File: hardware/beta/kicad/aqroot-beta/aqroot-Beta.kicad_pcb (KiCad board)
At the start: 4 copper layers, 74 x 155 mm, 187 parts, among them J1 CH280QV10-CT_50P, J2 Molex_5025700893, J3 USB_C_Receptacle_USB2.0_16P, J4 JST-PH-2 BATTERY, J5 COMMUNITY_HEADER_2x13, J6 JST-PH-2 SPEAKER, Q1 AO3400A, SW1 BOOT, SW2 UP, SW3 DOWN, SW4 LEFT, SW5 RIGHT, SW6 A_SELECT, SW7 B_BACK, SW8 HOME, SW9 SW_SPDT, U1 ESP32-S3-WROOM-1, U10 USBLC6-2SC6, U11 BQ25185, U12 TPS63020, U13 TPS61023, U14 MAX17048, U15 TPS22918, U16 TCA9517ADGK, U17 TPS61169DCKR, U2 TCA9535PWR, U3 TCA9535PWR, U4 BMI270, U5 MAX98357A, U6 TSOP38238, U7 E07-400M10S, U8 E22-900M22S, U9 ST25R3916-AQET

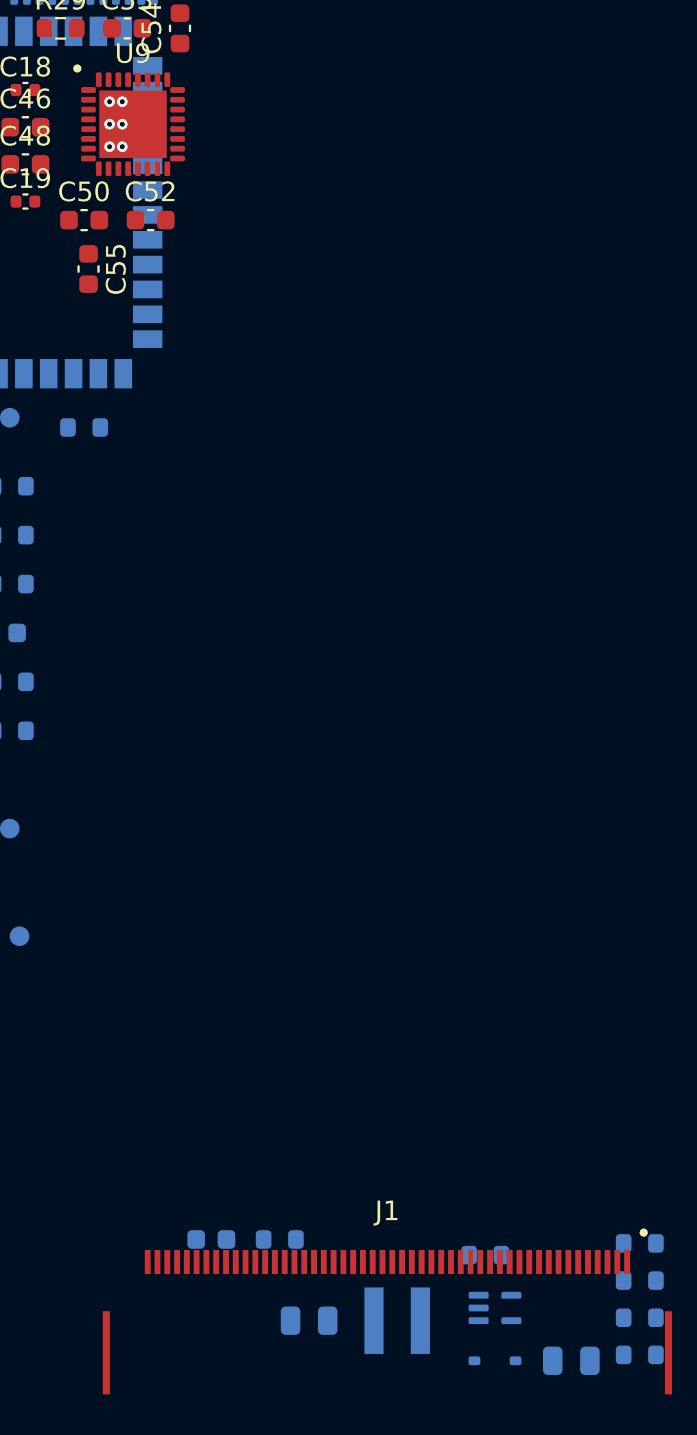
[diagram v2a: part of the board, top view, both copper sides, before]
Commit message: AQROOT Beta: close routing blockers, add U17 VIN bypass
Closes the three blockers from the Routing Pass 1 partial. No routing was
performed; GND remains the only net carrying copper.

BAT/SYS width lock, per CTO ruling. IBAT_OCP 3.125 A is a fault trip
threshold, not a routing design current, and the floor derived from it
made U11's 0.40 mm pitch west flank unroutable. BAT_MAIN min 1.00/opt
1.50 -> min 0.60/opt 1.00 mm (1.5 A sustained, 1 oz outer, dT=10 K needs
0.525 mm). SYS_MAIN min 0.60/opt 1.00 -> min 0.50/opt 0.80 mm. Netclass
defaults follow. The wrong derivation is corrected in the rule comment so
it stops propagating. Layer policy is now written into the file: both
rails are outer-layer by policy, BAT_MAIN must not distribute on In2
(1.5 A at 0.5 oz needs 2.73 mm), and an outer width must never be
inherited onto inner copper. Necking rule unchanged, still in the
PRECEDENCE TAIL. Zero RF/E4/E5 rule lines touched.

HEADER RESERVED In1 void removed. The audit found only J5 inside it - 26
THT pads, five of them GND - and no manufacturer requirement for an In1
void. Layer set F.Cu+In1+In2+B.Cu -> F.Cu+In2+B.Cu. In1 fill 10025.8 ->
10237.0 mm2, +211.3 mm2 (+2.11%), now 91.56% of outline. The 37 x 8.5 mm
slot in the reference plane is gone and J5's five GND pins now tie
directly to the pour. ST AN5240 Rev 5 section 4.2 corroborates: "avoiding
slots in the ground plane". J5 not moved. No new DRC issue.

U9 exposed-pad grounding audited against ST AN5240 Rev 5 section 8,
retrieved via browser because curl and WebFetch both fail against st.com,
and because the archived DS12484 datasheet has no layout guidance at all.
ST asks for the pad to be tied to the ground plane by "multiple
through-vias" to "keep the total parasitic inductance low", gives no
count and no pattern, and imposes no symmetry requirement on the thermal
pad - all seven symmetry mentions in AN5240 concern the RFO/RFI
differential traces and matching network. ST's Figure 16 shows 3x3 = 9
vias as a refer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
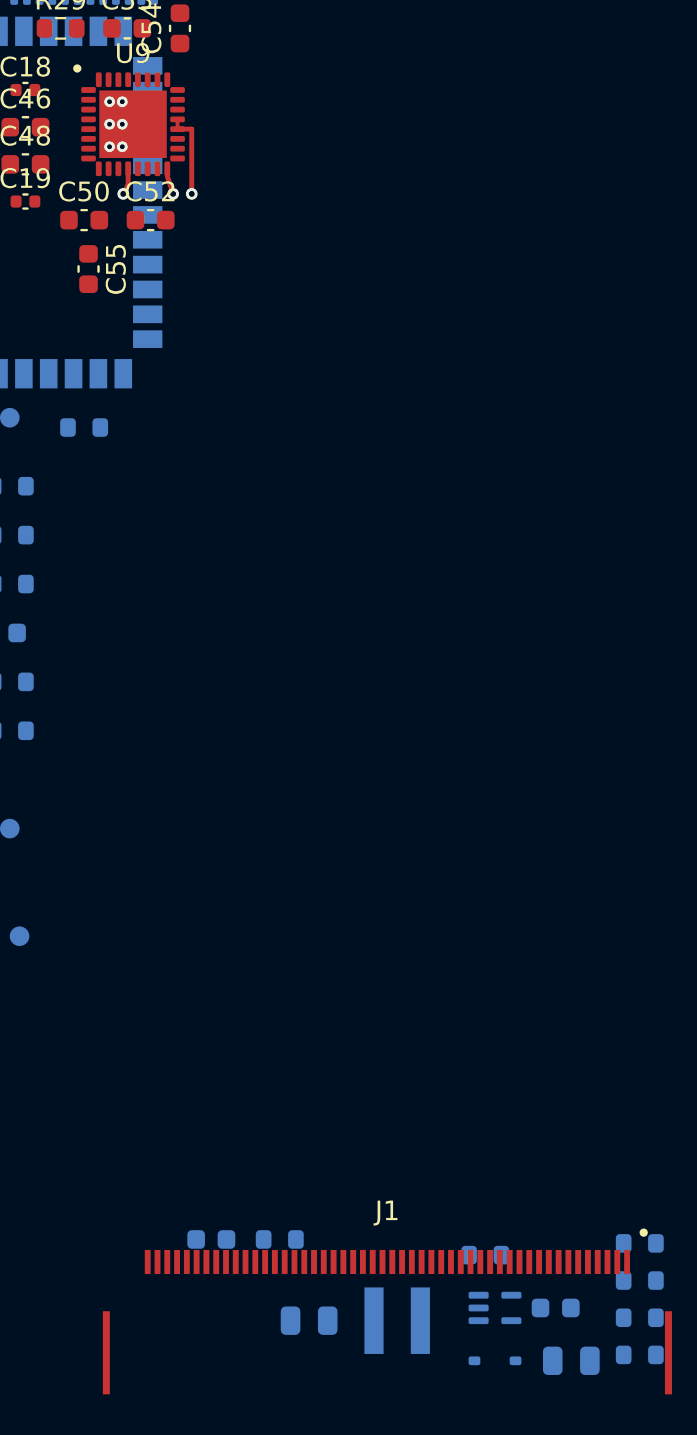
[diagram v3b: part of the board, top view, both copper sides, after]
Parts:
- added C56: 100nF, C_0603_1608Metric, B.Cu at (46.1, 82.5)
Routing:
- net GND: track 3.20 -> 9.67 mm, vias 18 -> 21
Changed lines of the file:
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@@
 	(footprint "C_0603_1608Metric"
 		(layer "F.Cu")
-		(at 22.225 29.4 -90)
+		(at 22 26.9)
 		(descr "Capacitor SMD 0603 (1608 Metric), square (rectangular) end terminal, IPC-7351 nominal, (Body size source: IPC-SM-782 page 76, https://www.pcb-3d.com/wordpress/wp-content/uploads/ipc-sm-782a_amendment_1_and_2.pdf)")
 		(tags "capacitor")
-		(property "Reference" "C55"
-			(at 0 -1.43 270)
+		(property "Reference" "C50"
+			(at 0 -1.43 0)
 			(layer "F.SilkS")
 			(effects
@@
 			)
 		)
-		(property "Value" "2.2uF"
-			(at 0 1.43 270)
+		(property "Value" "10nF"
+			(at 0 1.43 0)
 			(layer "F.Fab")
 			(effects
@@
 		)
 		(property "Datasheet" ""
-			(at 0 0 270)
+			(at 0 0 0)
 			(layer "F.Fab")
 			(hide yes)
@@
 		)
 		(property "Description" ""
-			(at 0 0 270)
+			(at 0 0 0)
 			(layer "F.Fab")
 			(hide yes)
@@
 		)
 		(property "KiLib_Generator" "SMD_2terminal_chip_molded"
-			(at 0 0 270)
+			(at 0 0 0)
 			(layer "F.SilkS")
 			(hide yes)
@@
 		(duplicate_pad_numbers_are_jumpers no)
 		(fp_line
-			(start -0.14058 0.51)
-			(end 0.14058 0.51)
+			(start -0.14058 -0.51)
+			(end 0.14058 -0.51)
 			(stroke
 				(width 0.12)
@@
 		)
 		(fp_line
-			(start -0.14058 -0.51)
-			(end 0.14058 -0.51)
+			(start -0.14058 0.51)
+			(end 0.14058 0.51)
 			(stroke
 				(width 0.12)
@@
 		)
 		(fp_text user "${REFERENCE}"
-			(at 0 0 270)
+			(at 0 0 0)
 			(layer "F.Fab")
 			(effects
@@
 		)
 		(pad "1" smd roundrect
-			(at -0.775 0 270)
+			(at -0.775 0)
 			(size 0.9 0.95)
 			(layers "F.Cu" "F.Mask" "F.Paste")
 			(roundrect_rratio 0.25)
-			(net "/NFC_5V_PA_PENDING")
+			(net "/04_SPI_B_RADIOS_NFC/NFC_VDD_RF")
 		)
 		(pad "2" smd roundrect
-			(at 0.775 0 270)
+			(at 0.775 0)
 			(size 0.9 0.95)
 			(layers "F.Cu" "F.Mask" "F.Paste")
@@
 	(footprint "C_0603_1608Metric"
 		(layer "F.Cu")
-		(at 22 26.9)
+		(at 22.225 29.4 -90)
 		(descr "Capacitor SMD 0603 (1608 Metric), square (rectangular) end terminal, IPC-7351 nominal, (Body size source: IPC-SM-782 page 76, https://www.pcb-3d.com/wordpress/wp-content/uploads/ipc-sm-782a_amendment_1_and_2.pdf)")
 		(tags "capacitor")
-		(property "Reference" "C50"
-			(at 0 -1.43 0)
+		(property "Reference" "C55"
+			(at 0 -1.43 270)
 			(layer "F.SilkS")
 			(effects
@@
 			)
 		)
-		(property "Value" "10nF"
-			(at 0 1.43 0)
+		(property "Value" "2.2uF"
+			(at 0 1.43 270)
 			(layer "F.Fab")
 			(effects
@@
 		)
 		(property "Datasheet" ""
-			(at 0 0 0)
+			(at 0 0 270)
 			(layer "F.Fab")
 			(hide yes)
@@
 		)
 		(property "Description" ""
-			(at 0 0 0)
+			(at 0 0 270)
 			(layer "F.Fab")
 			(hide yes)
@@
 		)
 		(property "KiLib_Generator" "SMD_2terminal_chip_molded"
-			(at 0 0 0)
+			(at 0 0 270)
 			(layer "F.SilkS")
 			(hide yes)
@@
 		(duplicate_pad_numbers_are_jumpers no)
 		(fp_line
-			(start -0.14058 -0.51)
-			(end 0.14058 -0.51)
+			(start -0.14058 0.51)
+			(end 0.14058 0.51)
 			(stroke
 				(width 0.12)
@@
 		)
 		(fp_line
-			(start -0.14058 0.51)
-			(end 0.14058 0.51)
+			(start -0.14058 -0.51)
+			(end 0.14058 -0.51)
 			(stroke
 				(width 0.12)
@@
 		)
 		(fp_text user "${REFERENCE}"
-			(at 0 0 0)
+			(at 0 0 270)
 			(layer "F.Fab")
 			(effects
@@
 		)
 		(pad "1" smd roundrect
-			(at -0.775 0)
+			(at -0.775 0 270)
 			(size 0.9 0.95)
 			(layers "F.Cu" "F.Mask" "F.Paste")
 			(roundrect_rratio 0.25)
-			(net "/04_SPI_B_RADIOS_NFC/NFC_VDD_RF")
+			(net "/NFC_5V_PA_PENDING")
 		)
 		(pad "2" smd roundrect
-			(at 0.775 0)
+			(at 0.775 0 270)
 			(size 0.9 0.95)
 			(layers "F.Cu" "F.Mask" "F.Paste")
@@
 		)
 	)
+	(footprint "C_0603_1608Metric"
+		(layer "B.Cu")
+		(at 46.1 82.5)
+		(descr "Capacitor SMD 0603 (1608 Metric), square (rectangular) end terminal, IPC-7351 nominal, (Body size source: IPC-SM-782 page 76, https://www.pcb-3d.com/wordpress/wp-content/uploads/ipc-sm-782a_amendment_1_and_2.pdf)")
+		(tags "capacitor")
+		(property "Reference" "C56"
+			(at 0 1.43 180)
+			(layer "B.SilkS")
+			(effects
+				(font
+					(size 1 1)
+					(thickness 0.15)
+				)
+				(justify mirror)
+			)
+		)
+		(property "Value" "100nF"
+			(at 0 -1.43 180)
+			(layer "B.Fab")
+			(effects
+				(font
+					(size 1 1)
+					(thickness 0.15)
+				)
+				(justify mirror)
+			)
+		)
+		(property "Datasheet" ""
+			(at 0 0 180)
+			(layer "B.Fab")
+			(hide yes)
+			(effects
+				(font
+					(size 1.27 1.27)
+				)
+				(justify mirror)
+			)
+		)
+		(property "Description" ""
+			(at 0 0 180)
+			(layer "B.Fab")
+			(hide yes)
+			(effects
+				(font
+					(size 1.27 1.27)
+				)
+				(justify mirror)
+			)
+		)
+		(property "KiLib_Generator" "SMD_2terminal_chip_molded"
+			(at 0 0 180)
+			(layer "B.SilkS")
+			(hide yes)
+			(effects
+				(font
+					(size 1 1)
+					(thickness 0.15)
+				)
+				(justify mirror)
+			)
+		)
+		(attr smd)
+		(duplicate_pad_numbers_are_jumpers no)
+		(fp_line
+			(start -0.14058 -0.51)
+			(end 0.14058 -0.51)
+			(stroke
+				(width 0.12)
+				(type solid)
+			)
+			(layer "B.SilkS")
+		)
+		(fp_line
+			(start -0.14058 0.51)
+			(end 0.14058 0.51)
+			(stroke
+				(width 0.12)
+				(type solid)
+			)
+			(layer "B.SilkS")
+		)
+		(fp_rect
+			(start -1.48 0.73)
+			(end 1.48 -0.73)
+			(stroke
+				(width 0.05)
+				(type solid)
+			)
+			(fill no)
+			(layer "B.CrtYd")
+		)
+		(fp_rect
+			(start -0.8 0.4)
+			(end 0.8 -0.4)
+			(stroke
+				(width 0.1)
+				(type solid)
+			)
+			(fill no)
+			(layer "B.Fab")
+		)
+		(fp_text user "${REFERENCE}"
+			(at 0 0 180)
+			(layer "B.Fab")
+			(effects
+				(font
+					(size 0.4 0.4)
+					(thickness 0.06)
+				)
+				(justify mirror)
+			)
+		)
+		(pad "1" smd roundrect
+			(at -0.775 0)
+			(size 0.9 0.95)
+			(layers "B.Cu" "B.Mask" "B.Paste")
+			(roundrect_rratio 0.25)
+			(net "+3V3")
+		)
+		(pad "2" smd roundrect
+			(at 0.775 0)
+			(size 0.9 0.95)
+			(layers "B.Cu" "B.Mask" "B.Paste")
+			(roundrect_rratio 0.25)
+			(net "GND")
+		)
+		(embedded_fonts no)
+		(model "${KICAD10_3DMODEL_DIR}/Capacitor_SMD.3dshapes/C_0603_1608Metric.step"
+			(offset
+				(xyz 0 0 0)
+			)
+			(scale
+				(xyz 1 1 1)
+			)
+			(rotate
+				(xyz 0 0 0)
+			)
+		)
+	)
 	(footprint "Resistor_SMD:R_0603_1608Metric"
 		(layer "B.Cu")
@@
 	)
 	(segment
+		(start 24.25 24.65)
+		(end 24.25 25.1)
+		(width 0.25)
+		(layer "F.Cu")
+		(net "GND")
+	)
+	(segment
 		(start 63.9 67.4)
 		(end 63.9 67.8)
@@
 	)
 	(segment
+		(start 26.775 22.25)
+		(end 27.5 22.25)
+		(width 0.25)
+		(layer "F.Cu")
+		(net "GND")
+	)
+	(segment
 		(start 64.5 52.4)
 		(end 64.5 53.9)
@@
 	)
 	(segment
+		(start 26.775 21.75)
+		(end 26.775 22.25)
+		(width 0.2)
+		(layer "F.Cu")
+		(net "GND")
+	)
+	(segment
 		(start 63.9 67.8)
 		(end 62.6 67.8)
@@
 		(net "GND")
 	)
+	(segment
+		(start 24.25 25.1)
+		(end 24 25.56)
+		(width 0.25)
+		(layer "F.Cu")
+		(net "GND")
+	)
+	(segment
+		(start 26.25 24.65)
+		(end 26.55 25.56)
+		(width 0.25)
+		(layer "F.Cu")
+		(net "GND")
+	)
+	(segment
+		(start 27.5 22.25)
+		(end 27.5 25.56)
+		(width 0.25)
+		(layer "F.Cu")
+		(net "GND")
+	)
 	(via
 		(at 62.5 14.8)
@@
 	)
 	(via
+		(at 27.5 25.56)
+		(size 0.6)
+		(drill 0.3)
+		(layers "F.Cu" "B.Cu")
+		(net "GND")
+	)
+	(via
 		(at 64.5 80.5)
 		(size 0.55)
@@
 	)
 	(via
+		(at 24 25.56)
+		(size 0.6)
+		(drill 0.3)
+		(layers "F.Cu" "B.Cu")
+		(net "GND")
+	)
+	(via
 		(at 65.5 50.65)
 		(size 0.55)
@@
 		(net "GND")
 	)
+	(via
+		(at 26.55 25.56)
+		(size 0.6)
+		(drill 0.3)
+		(layers "F.Cu" "B.Cu")
+		(net "GND")
+	)
 	(zone
 		(layers "F.Cu" "B.Cu" "In1.Cu" "In2.Cu")
-		(name "HEADER RESERVED")
+		(name "NFC RESERVED")
 		(hatch edge 0.5)
 		(connect_pads
@@
 		(polygon
 			(pts
-				(xy 18.5 0) (xy 55.5 0) (xy 55.5 8.5) (xy 18.5 8.5)
+				(xy 28 15) (xy 54 15) (xy 54 35) (xy 28 35)
 			)
 		)
@@
 	(zone
 		(layers "F.Cu" "B.Cu" "In1.Cu" "In2.Cu")
-		(name "NFC RESERVED")
+		(name "WROOM ANTENNA KEEPOUT")
 		(hatch edge 0.5)
 		(connect_pads
@@
 			(tracks not_allowed)
 			(vias not_allowed)
-			(pads allowed)
+			(pads not_allowed)
 			(copperpour not_allowed)
 			(footprints allowed)
@@
 		(polygon
 			(pts
-				(xy 28 15) (xy 54 15) (xy 54 35) (xy 28 35)
+				(xy 0 17) (xy 6 17) (xy 6 35) (xy 0 35)
 			)
 		)
 	)
 	(zone
-		(layers "F.Cu" "B.Cu" "In1.Cu" "In2.Cu")
-		(name "WROOM ANTENNA KEEPOUT")
+		(layers "F.Cu" "B.Cu" "In2.Cu")
+		(name "HEADER RESERVED")
 		(hatch edge 0.5)
 		(connect_pads
@@
 			(tracks not_allowed)
 			(vias not_allowed)
-			(pads not_allowed)
+			(pads allowed)
 			(copperpour not_allowed)
 			(footprints allowed)
@@
 		(polygon
 			(pts
-				(xy 0 17) (xy 6 17) (xy 6 35) (xy 0 35)
+				(xy 18.5 0) (xy 55.5 0) (xy 55.5 8.5) (xy 18.5 8.5)
 			)
 		)

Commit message: AQROOT Beta: set C56 to 1 uF for TI-compliant local CIN
C56 100 nF -> 1 uF, keeping ref, footprint, position (46.100, 82.500),
rotation 0, B.Cu side and nets (+3V3 / GND). No capacitor added.

TI SNVSA40B section 7.5.1 requires the input capacitor close to the VIN
and GND pins, and Recommended Operating Conditions give CI minimum 1 uF.
100 nF was useful HF bypassing but did not satisfy that literally. C43
4.7 uF remains the power-stage reservoir next to L3 at 2.37 mm; C56 is
now the local U17 VIN capacitor at 1.624 mm from pin 5.

BOM stays a multi-source commodity passive: 1 uF, 16 V, X7R, 0603, exact
MPN deferred to BOM verification, which must confirm the production part
keeps reasonable effective capacitance at 3.3 V DC bias.

Verified: schematic netlist topology byte-identical (174 nets, same node
sets); PCB footprint Value synchronised so parity gains nothing; DRC 0
errors, 234 warnings; ERC 116/58 excluded/58 live, zero delta; placement
188 footprints unchanged.

Co-Authored-By: Claude Opus 5 <noreply@anthropic.com>
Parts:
- C56: value 100nF -> 1uF
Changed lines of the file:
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@@
 			)
 		)
-		(property "Value" "100nF"
+		(property "Value" "1uF"
 			(at 0 -1.43 180)
 			(layer "B.Fab")
